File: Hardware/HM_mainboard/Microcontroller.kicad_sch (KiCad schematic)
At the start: 17 parts, among them J2 USB4105-GF-A, J3 Conn_01x04, U3 ESP32-S3-WROOM-1, Y1 32.768 kHz

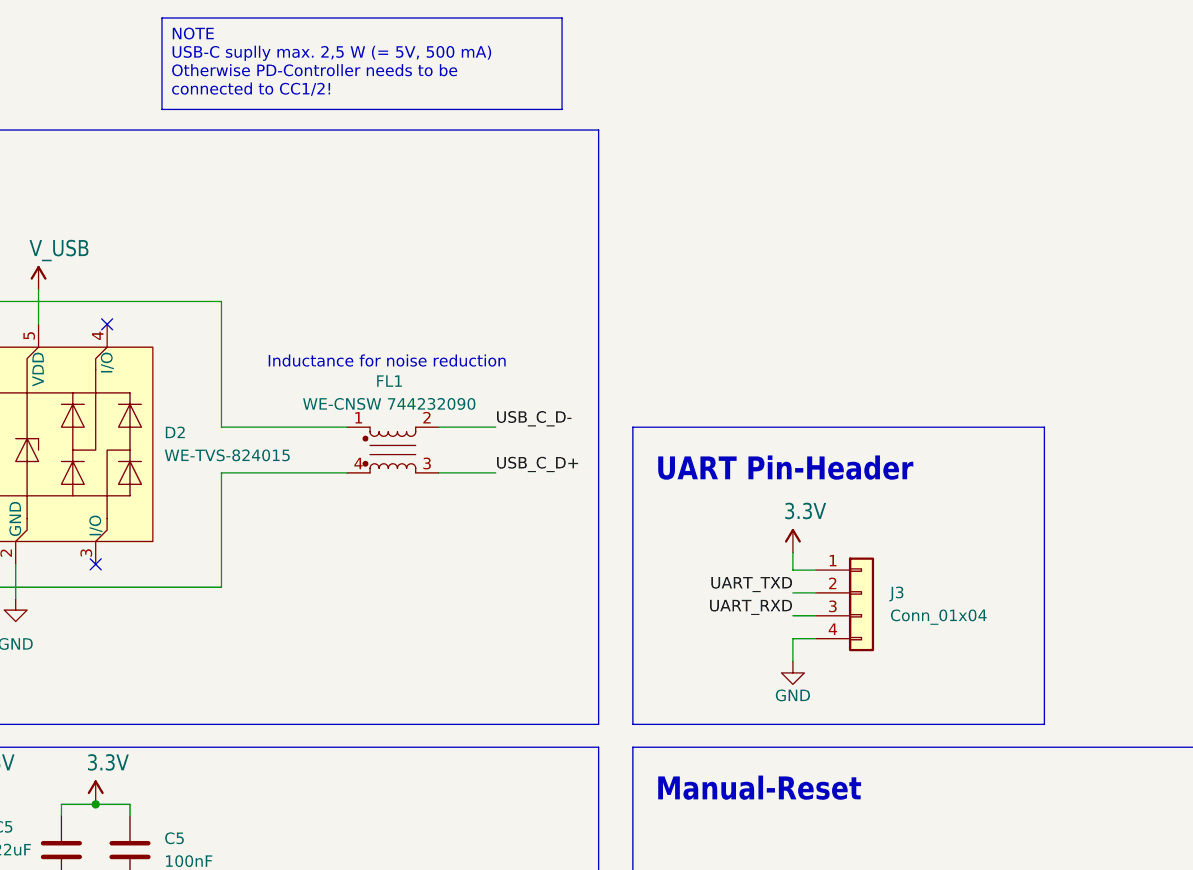
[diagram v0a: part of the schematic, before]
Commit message: Added testpoints to pcb
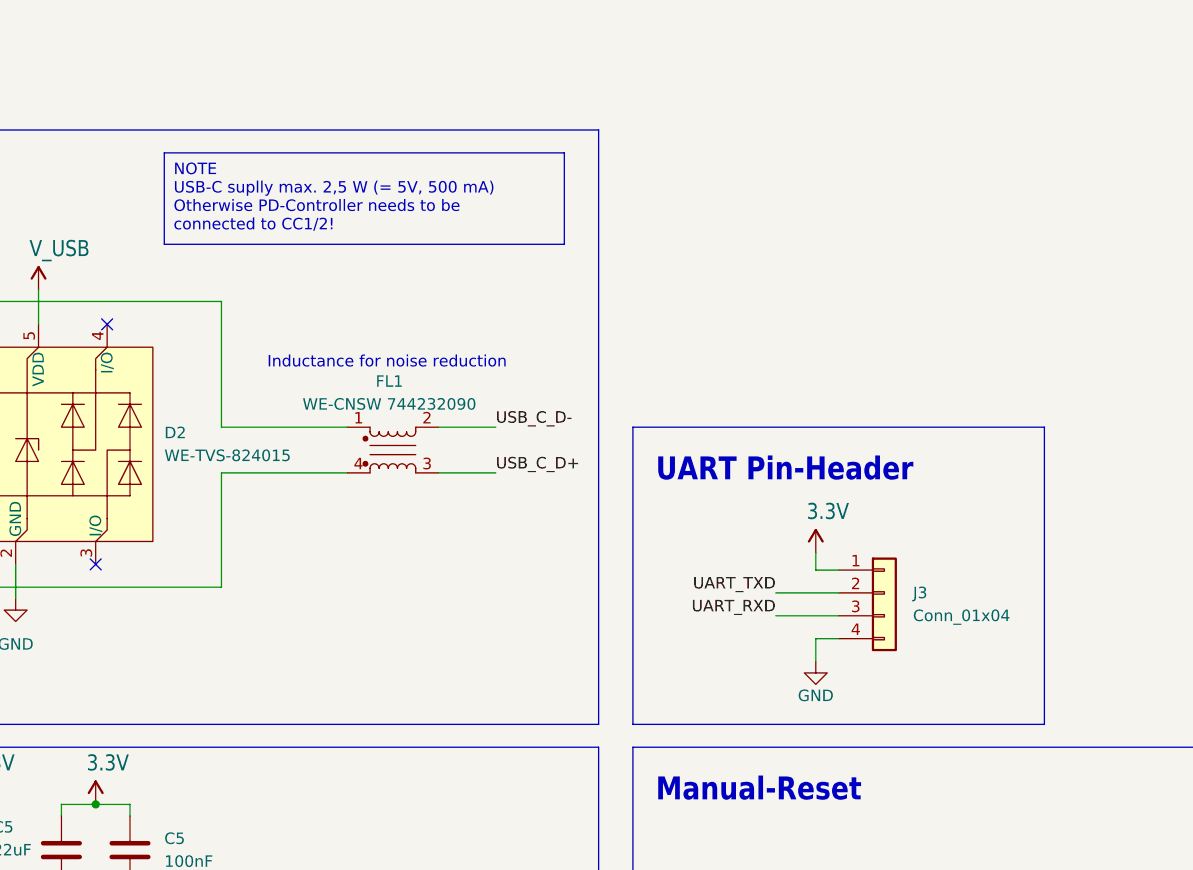
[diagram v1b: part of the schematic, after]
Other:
- moved on the sheet: J3
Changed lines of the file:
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@@
     (stroke (width 0) (type default))
   )
-  (wire (pts (xy 195.58 62.23) (xy 195.58 64.135))
+  (wire (pts (xy 198.12 62.23) (xy 198.12 64.135))
     (stroke (width 0) (type default))
   )
@@
     (stroke (width 0) (type default))
   )
+  (wire (pts (xy 193.675 69.215) (xy 200.66 69.215))
+    (stroke (width 0) (type default))
+  )
   (wire (pts (xy 43.18 72.39) (xy 43.18 73.66))
     (stroke (width 0) (type default))
@@
     (stroke (width 0) (type default))
   )
+  (wire (pts (xy 193.675 66.675) (xy 200.66 66.675))
+    (stroke (width 0) (type default))
+  )
   (wire (pts (xy 151.13 139.7) (xy 153.67 139.7))
     (stroke (width 0) (type default))
@@
     (stroke (width 0) (type default))
   )
-  (wire (pts (xy 195.58 64.135) (xy 198.12 64.135))
-    (stroke (width 0) (type default))
-  )
-  (wire (pts (xy 195.58 66.675) (xy 198.12 66.675))
+  (wire (pts (xy 198.12 64.135) (xy 200.66 64.135))
     (stroke (width 0) (type default))
   )
@@
     (stroke (width 0) (type default))
   )
-  (wire (pts (xy 195.58 71.755) (xy 198.12 71.755))
-    (stroke (width 0) (type default))
-  )
-  (wire (pts (xy 195.58 74.295) (xy 195.58 71.755))
+  (wire (pts (xy 198.12 71.755) (xy 200.66 71.755))
+    (stroke (width 0) (type default))
+  )
+  (wire (pts (xy 198.12 74.295) (xy 198.12 71.755))
     (stroke (width 0) (type default))
   )
@@
     (stroke (width 0) (type default))
   )
-  (wire (pts (xy 195.58 69.215) (xy 198.12 69.215))
-    (stroke (width 0) (type default))
-  )
   (wire (pts (xy 86.36 66.04) (xy 101.6 66.04))
     (stroke (width 0) (type default))
@@
   )
   (text_box "NOTE\nUSB-C suplly max. 2,5 W (= 5V, 500 mA)\nOtherwise PD-Controller needs to be connected to CC1/2!\n\n"
-    (at 125.476 2.794 0) (size 44.45 10.16)
+    (at 125.73 17.78 0) (size 44.45 10.16)
     (stroke (width 0) (type default))
     (fill (type color) (color 255 165 125 1))
@@
     (effects (font (size 1.27 1.27)) (justify left bottom))
   )
-  (label "UART_RXD" (at 195.58 69.215 180) (fields_autoplaced)
+  (label "UART_RXD" (at 193.675 69.215 180) (fields_autoplaced)
     (effects (font (size 1.27 1.27)) (justify right bottom))
   )
@@
     (effects (font (size 1.27 1.27)) (justify left bottom))
   )
-  (label "UART_TXD" (at 195.58 66.675 180) (fields_autoplaced)
+  (label "UART_TXD" (at 193.675 66.675 180) (fields_autoplaced)
     (effects (font (size 1.27 1.27)) (justify right bottom))
   )
@@
     )
   )
-  (symbol (lib_name "GND_1") (lib_id "power:GND") (at 195.58 74.295 0) (unit 1)
+  (symbol (lib_name "GND_1") (lib_id "power:GND") (at 198.12 74.295 0) (unit 1)
     (in_bom yes) (on_board yes) (dnp no)
-    (property "Reference" "#PWR06" (at 195.58 80.645 0)
-      (effects (font (size 1.27 1.27)) hide)
-    )
-    (property "Value" "GND" (at 195.58 78.105 0)
+    (property "Reference" "#PWR06" (at 198.12 80.645 0)
+      (effects (font (size 1.27 1.27)) hide)
+    )
+    (property "Value" "GND" (at 198.12 78.105 0)
       (effects (font (size 1.27 1.27)))
     )
-    (property "Footprint" "" (at 195.58 74.295 0)
-      (effects (font (size 1.27 1.27)) hide)
-    )
-    (property "Datasheet" "" (at 195.58 74.295 0)
+    (property "Footprint" "" (at 198.12 74.295 0)
+      (effects (font (size 1.27 1.27)) hide)
+    )
+    (property "Datasheet" "" (at 198.12 74.295 0)
       (effects (font (size 1.27 1.27)) hide)
     )
@@
     )
   )
-  (symbol (lib_id "esp32-thing-eagle-import:3.3V") (at 195.58 62.23 0) (unit 1)
+  (symbol (lib_id "esp32-thing-eagle-import:3.3V") (at 198.12 62.23 0) (unit 1)
     (in_bom yes) (on_board yes) (dnp no)
-    (property "Reference" "#SUPPLY08" (at 195.58 62.23 0)
-      (effects (font (size 1.27 1.27)) hide)
-    )
-    (property "Value" "3.3V" (at 194.564 58.674 0)
+    (property "Reference" "#SUPPLY08" (at 198.12 62.23 0)
+      (effects (font (size 1.27 1.27)) hide)
+    )
+    (property "Value" "3.3V" (at 197.104 58.674 0)
       (effects (font (size 1.778 1.5113)) (justify left bottom))
     )
-    (property "Footprint" "" (at 195.58 62.23 0)
-      (effects (font (size 1.27 1.27)) hide)
-    )
-    (property "Datasheet" "" (at 195.58 62.23 0)
+    (property "Footprint" "" (at 198.12 62.23 0)
+      (effects (font (size 1.27 1.27)) hide)
+    )
+    (property "Datasheet" "" (at 198.12 62.23 0)
       (effects (font (size 1.27 1.27)) hide)
     )
@@
     )
   )
-  (symbol (lib_id "Connector_Generic:Conn_01x04") (at 203.2 66.675 0) (unit 1)
+  (symbol (lib_id "Connector_Generic:Conn_01x04") (at 205.74 66.675 0) (unit 1)
     (in_bom yes) (on_board yes) (dnp no) (fields_autoplaced)
-    (property "Reference" "J3" (at 206.375 66.675 0)
+    (property "Reference" "J3" (at 208.915 66.675 0)
       (effects (font (size 1.27 1.27)) (justify left))
     )
-    (property "Value" "Conn_01x04" (at 206.375 69.215 0)
+    (property "Value" "Conn_01x04" (at 208.915 69.215 0)
       (effects (font (size 1.27 1.27)) (justify left))
     )
-    (property "Footprint" "Connector_PinHeader_2.54mm:PinHeader_1x04_P2.54mm_Vertical" (at 203.2 66.675 0)
-      (effects (font (size 1.27 1.27)) hide)
-    )
-    (property "Datasheet" "~" (at 203.2 66.675 0)
-      (effects (font (size 1.27 1.27)) hide)
-    )
-    (property "Reichelt" "" (at 203.2 66.675 0)
-      (effects (font (size 1.27 1.27)) hide)
-    )
-    (property "Mouser" "Beliebige Stiftleiste, Raster: 2.54mm" (at 203.2 66.675 0)
-      (effects (font (size 1.27 1.27)) hide)
-    )
+    (property "Footprint" "Connector_PinHeader_2.54mm:PinHeader_1x04_P2.54mm_Vertical" (at 205.74 66.675 0)
+      (effects (font (size 1.27 1.27)) hide)
+    )
+    (property "Datasheet" "~" (at 205.74 66.675 0)
+      (effects (font (size 1.27 1.27)) hide)
+    )
+    (property "Reichelt" "" (at 205.74 66.675 0)
+      (effects (font (size 1.27 1.27)) hide)
+    )
+    (property "Mouser" "Beliebige Stiftleiste, Raster: 2.54mm" (at 205.74 66.675 0)
+      (effects (font (size 1.27 1.27)) hide)
+    )

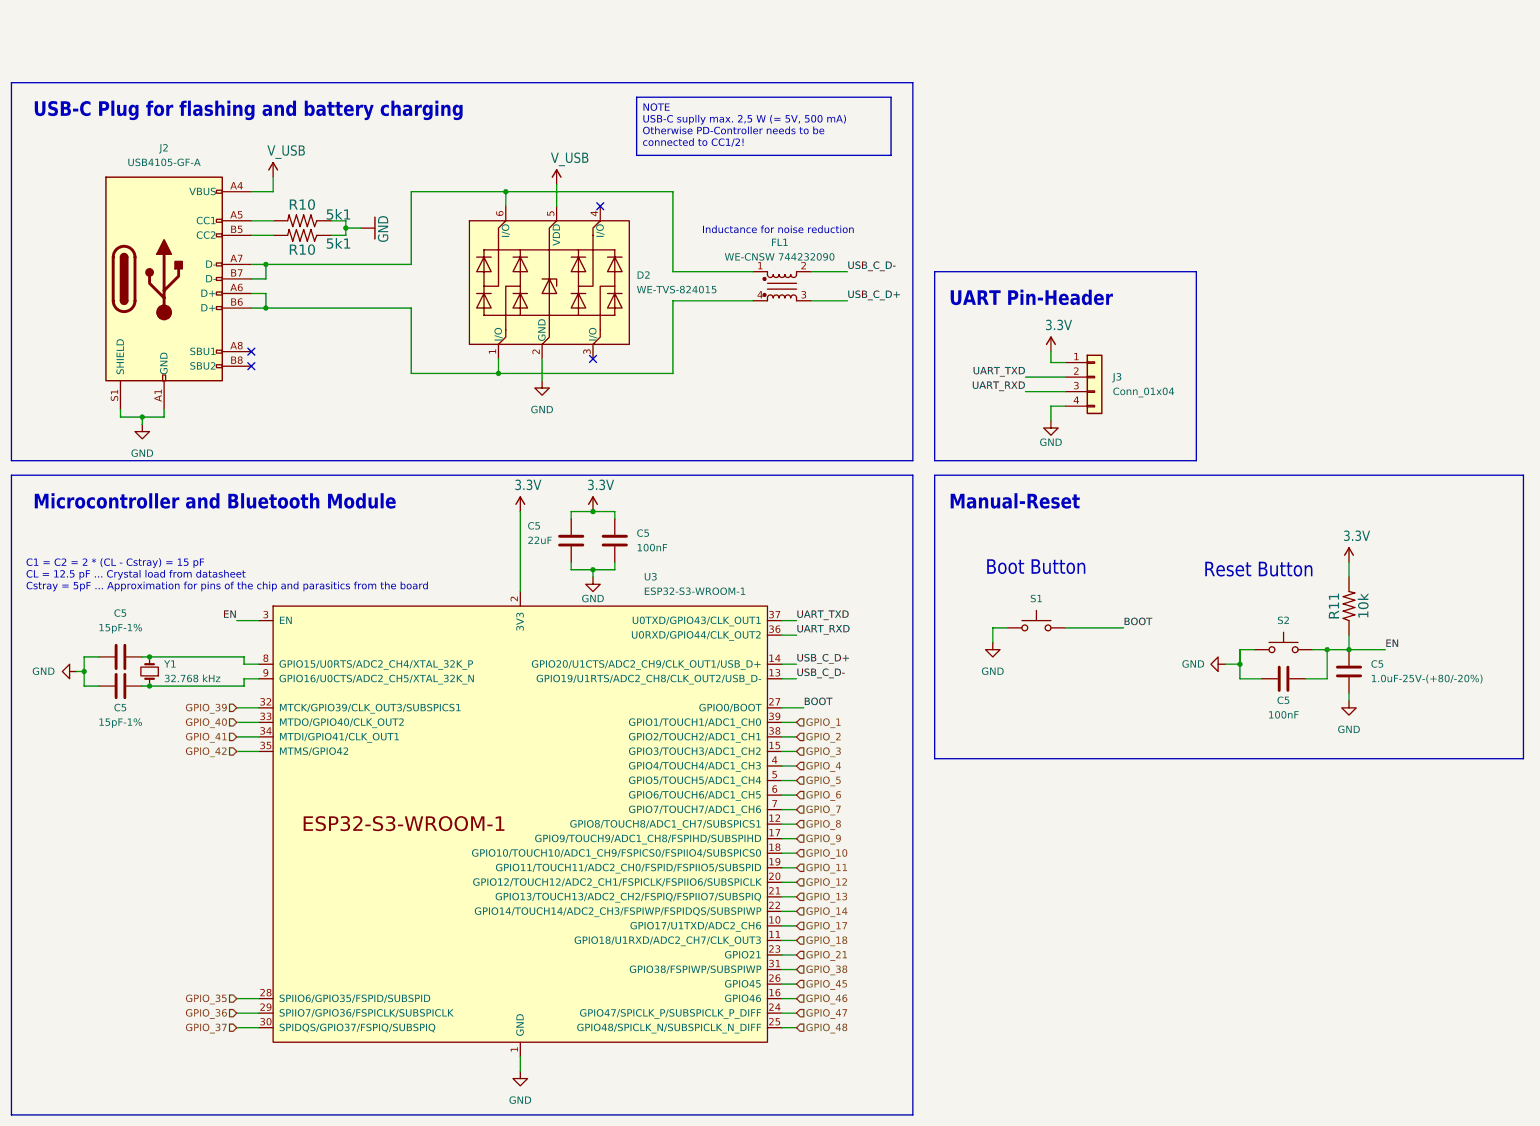
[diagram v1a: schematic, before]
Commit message: Updated schematic and PCB according to Email from BA on 16th of April
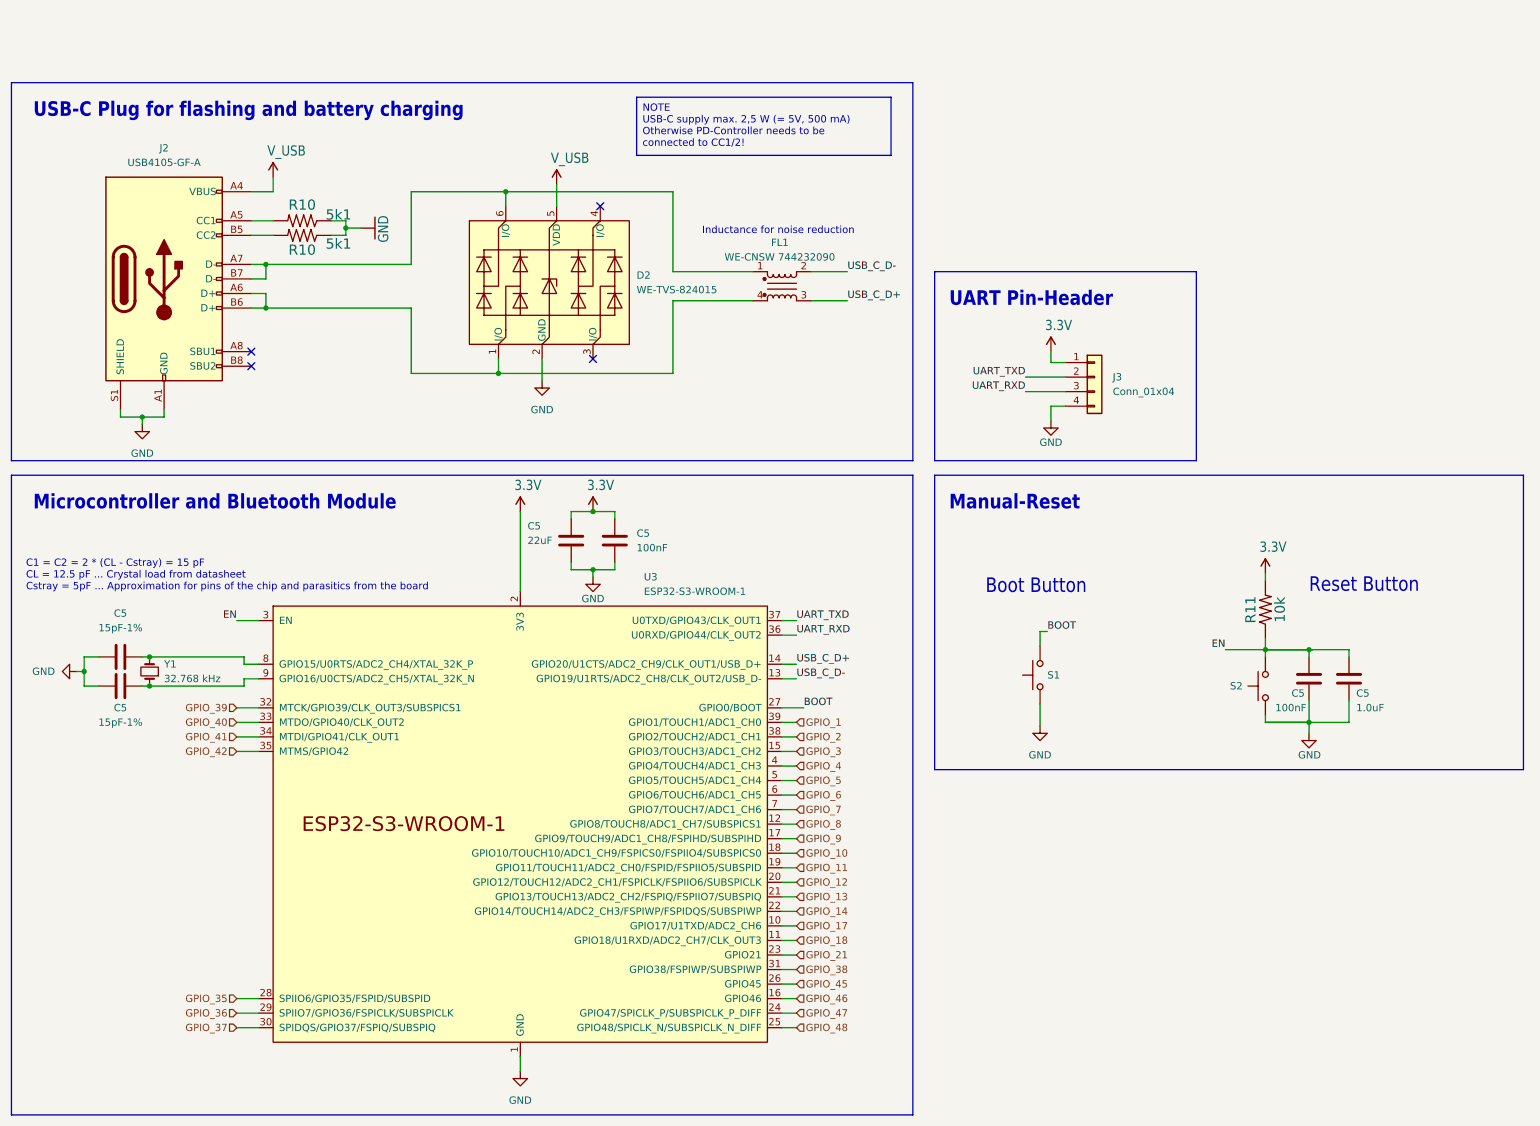
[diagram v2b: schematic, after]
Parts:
- C5: value 1.0uF-25V-(+80/-20%) -> 1.0uF
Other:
- moved on the sheet: C5, R11, S1, S2

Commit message: Updated schematic to version v2.0.0
•	Removed two 6-Axis IMUs
•	As the BNO055 did not respond to I2C requests, a 2k7 pullup was added in parallel to the I2C-SDA pullup. The behavior is described here:  https://forums.adafruit.com/viewtopic.php?t=205215
•	Added mounting holes for enclosure
•	Added board description prints
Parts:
- added R15: 1k8, Resistor_SMD:R_0603_1608Metric_Pad0.98x0.95mm_HandSolder, symbol esp32-thing-eagle-import:10KOHM-1/10W-1%(0603)0603
- added R16: 4k7, Resistor_SMD:R_0603_1608Metric_Pad0.98x0.95mm_HandSolder, symbol esp32-thing-eagle-import:10KOHM-1/10W-1%(0603)0603
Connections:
- net 3.3V: now also R15.2, R16.2
- net GPIO_1: no longer names the net of U3.39 (GPIO1/TOUCH1/ADC1_CH0)
- net GPIO_10 renamed I2C_SDA
- net I2C_SDA: now also R15.1
- net GPIO_11: no longer names the net of U3.19 (GPIO11/TOUCH11/ADC2_CH0/FSPID/FSPIIO5/SUBSPID)
- net GPIO_12: no longer names the net of U3.20 (GPIO12/TOUCH12/ADC2_CH1/FSPICLK/FSPIIO6/SUBSPICLK)
- net GPIO_13 renamed BNO055_INT
- net GPIO_14 renamed MPRLS_INT
- net GPIO_17 renamed LED_STAT_R
- net GPIO_18 renamed LED_STAT_G
- net GPIO_2: no longer names the net of U3.38 (GPIO2/TOUCH2/ADC1_CH1)
- net GPIO_21: no longer names the net of U3.23 (GPIO21)
- net GPIO_3: no longer names the net of U3.15 (GPIO3/TOUCH3/ADC1_CH2)
- net GPIO_35: no longer names the net of U3.28 (SPIIO6/GPIO35/FSPID/SUBSPID)
- net GPIO_36: no longer names the net of U3.29 (SPIIO7/GPIO36/FSPICLK/SUBSPICLK)
- net GPIO_37: no longer names the net of U3.30 (SPIDQS/GPIO37/FSPIQ/SUBSPIQ)
- net GPIO_38: no longer names the net of U3.31 (GPIO38/FSPIWP/SUBSPIWP)
- net GPIO_39 renamed BTN_4
- net GPIO_4 renamed V_BAT_MEASURE
- net GPIO_40 renamed BTN_3
- net GPIO_41 renamed BTN_2
- net GPIO_42 renamed BTN_1
- net GPIO_45: no longer names the net of U3.26 (GPIO45)
- net GPIO_46: no longer names the net of U3.16 (GPIO46)
- net GPIO_47: no longer names the net of U3.24 (GPIO47/SPICLK_P/SUBSPICLK_P_DIFF)
- net GPIO_48: no longer names the net of U3.25 (GPIO48/SPICLK_N/SUBSPICLK_N_DIFF)
- net GPIO_5 renamed BAT_CHRG_STATUS
- net GPIO_6 renamed LED_BAT_R
- net GPIO_7 renamed LED_BAT_G
- net GPIO_8: no longer names the net of U3.12 (GPIO8/TOUCH8/ADC1_CH7/SUBSPICS1)
- net GPIO_9 renamed I2C_SCL
- net I2C_SCL: now also R16.1
- no-connect marks 4 -> 19
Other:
- note added: "1k8 resistor at I2C-SDA line because of I2C-timing issues with BNO055."
- note added: "I2C-Pullup"
- moved on the sheet: C5, J3, R11, S1, S2
